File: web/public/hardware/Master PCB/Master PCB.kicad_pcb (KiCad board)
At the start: 2 copper layers, 73.5 x 77.1 mm, 110 parts, among them J1 SWD Conn, J10 LED3, J11 LDR4, J12 LED4, J13 LED Conn, J14 Relay Conn, J2 OLED1, J3 OLED2, J4 5V_IN, J5 LDR1, J6 LED1, J7 LDR2, J8 LED2, J9 LDR3, Q1 2N7000, Q2 2N7000, Q3 2N7000, Q4 2N7000, SW1 nRST, SW2 Menu Encoder, U1 STM32U585VITx, U2 M95P32-IXMNT, U3 TLV62568DBV, U4 LM339

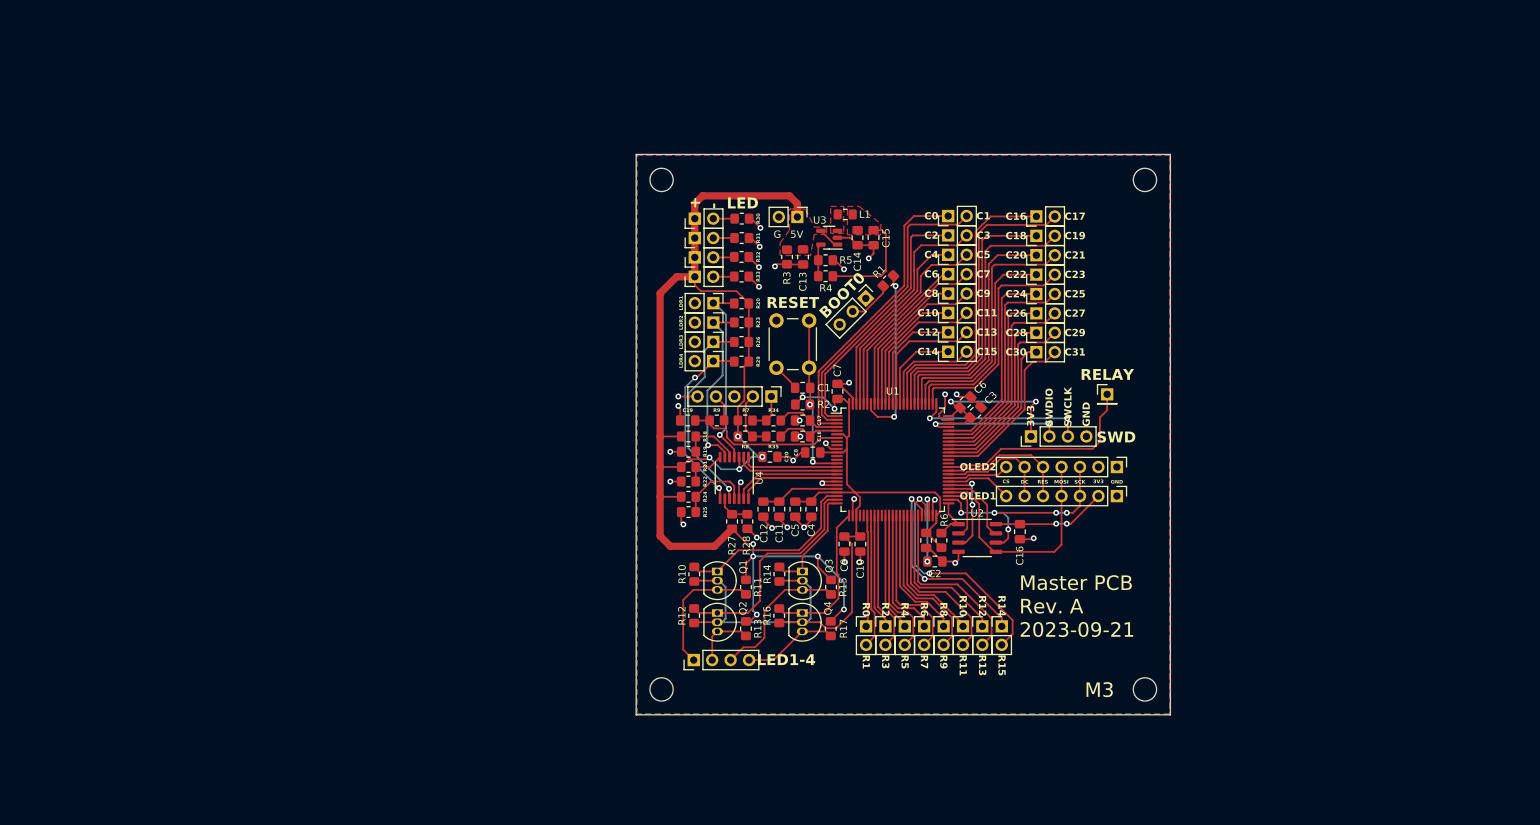
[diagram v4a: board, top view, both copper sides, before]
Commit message: Change STM32 pinout, begin placing components on new PCB
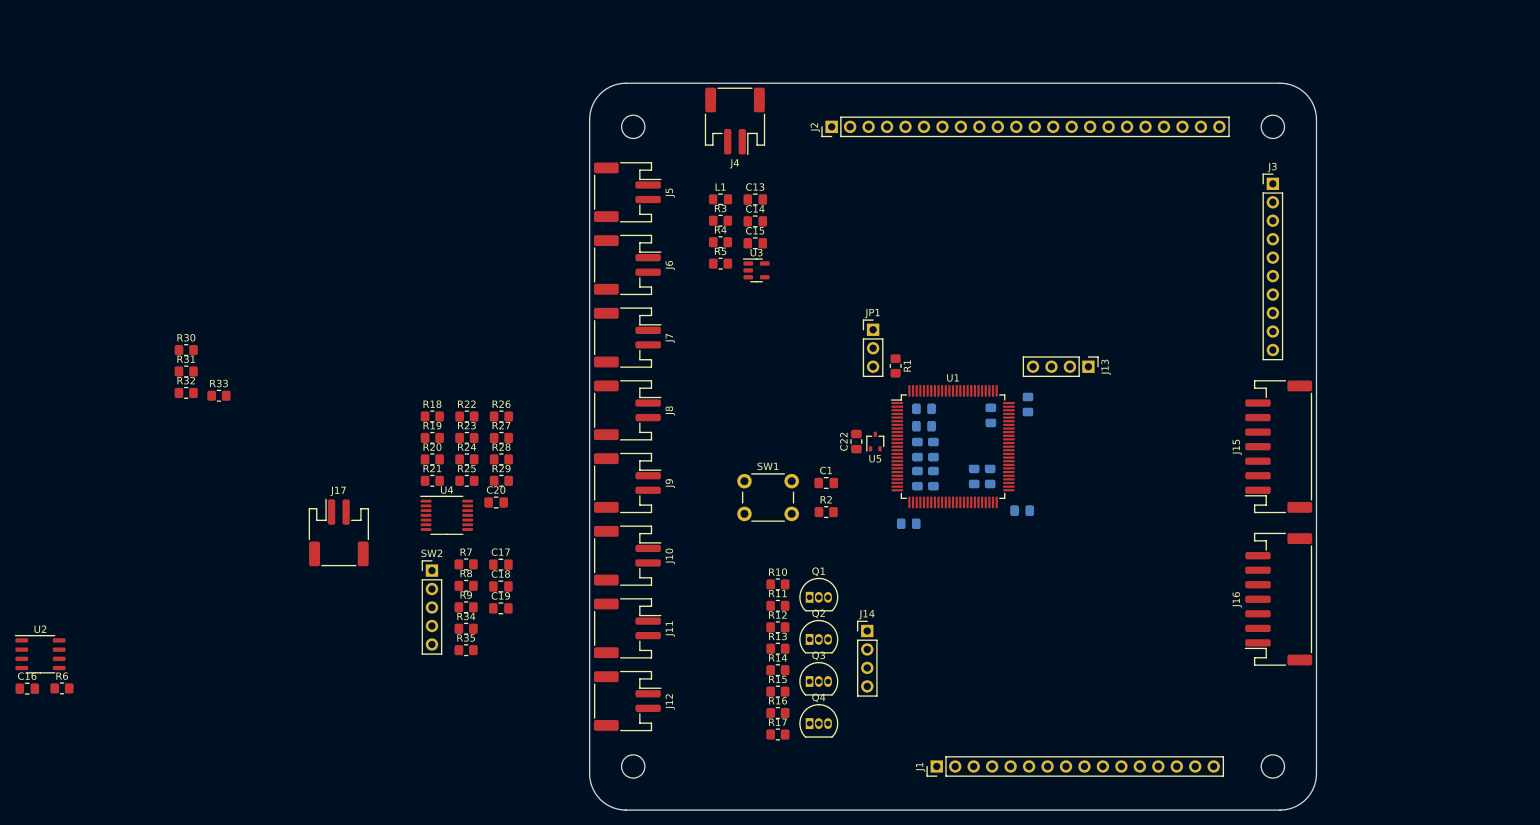
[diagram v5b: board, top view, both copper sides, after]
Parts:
- removed COL1: Cols 0-1, Connector_PinHeader_2.54mm:PinHeader_1x02_P2.54mm_Vertical
- removed COL10: Cols 18-19, Connector_PinHeader_2.54mm:PinHeader_1x02_P2.54mm_Vertical
- removed COL11: Cols 20-21, Connector_PinHeader_2.54mm:PinHeader_1x02_P2.54mm_Vertical
- removed COL12: Cols 22-23, Connector_PinHeader_2.54mm:PinHeader_1x02_P2.54mm_Vertical
- removed COL13: Cols 24-25, Connector_PinHeader_2.54mm:PinHeader_1x02_P2.54mm_Vertical
- removed COL14: Cols 26-27, Connector_PinHeader_2.54mm:PinHeader_1x02_P2.54mm_Vertical
- removed COL15: Cols 28-29, Connector_PinHeader_2.54mm:PinHeader_1x02_P2.54mm_Vertical
- removed COL16: Cols 30-31, Connector_PinHeader_2.54mm:PinHeader_1x02_P2.54mm_Vertical
- removed COL2: Cols 2-3, Connector_PinHeader_2.54mm:PinHeader_1x02_P2.54mm_Vertical
- removed COL3: Cols 4-5, Connector_PinHeader_2.54mm:PinHeader_1x02_P2.54mm_Vertical
- removed COL4: Cols 6-7, Connector_PinHeader_2.54mm:PinHeader_1x02_P2.54mm_Vertical
- removed COL5: Cols 8-9, Connector_PinHeader_2.54mm:PinHeader_1x02_P2.54mm_Vertical
- removed COL6: Cols 10-11, Connector_PinHeader_2.54mm:PinHeader_1x02_P2.54mm_Vertical
- removed COL7: Cols 12-13, Connector_PinHeader_2.54mm:PinHeader_1x02_P2.54mm_Vertical
- removed COL8: Cols 14-15, Connector_PinHeader_2.54mm:PinHeader_1x02_P2.54mm_Vertical
- removed COL9: Cols 16-17, Connector_PinHeader_2.54mm:PinHeader_1x02_P2.54mm_Vertical
- removed ROW1: Rows 0-1, Connector_PinHeader_2.54mm:PinHeader_1x02_P2.54mm_Vertical
- removed ROW2: Rows 2-3, Connector_PinHeader_2.54mm:PinHeader_1x02_P2.54mm_Vertical
- removed ROW3: Rows 4-5, Connector_PinHeader_2.54mm:PinHeader_1x02_P2.54mm_Vertical
- removed ROW4: Rows 6-7, Connector_PinHeader_2.54mm:PinHeader_1x02_P2.54mm_Vertical
- removed ROW5: Rows 8-9, Connector_PinHeader_2.54mm:PinHeader_1x02_P2.54mm_Vertical
- removed ROW6: Rows 10-11, Connector_PinHeader_2.54mm:PinHeader_1x02_P2.54mm_Vertical
- removed ROW7: Rows 12-13, Connector_PinHeader_2.54mm:PinHeader_1x02_P2.54mm_Vertical
- removed ROW8: Rows 14-15, Connector_PinHeader_2.54mm:PinHeader_1x02_P2.54mm_Vertical
- added C22: 100nF, Capacitor_SMD:C_0805_2012Metric_Pad1.18x1.45mm_HandSolder, F.Cu at (136.7, 99.3)
- added J15: OLED1, Connector_JST:JST_PH_S7B-PH-SM4-TB_1x07-1MP_P2.00mm_Horizontal, F.Cu at (194.8, 100.0)
- added J16: OLED2, Connector_JST:JST_PH_S7B-PH-SM4-TB_1x07-1MP_P2.00mm_Horizontal, F.Cu at (194.8, 121.0)
- added J17: Relay Conn, Connector_JST:JST_PH_S2B-PH-SM4-TB_1x02-1MP_P2.00mm_Horizontal, F.Cu at (65.5, 111.8)
- added U5: MAX7375AXR805, Package_TO_SOT_SMD:SOT-323_SC-70, F.Cu at (139.3, 99.3)
- C10, C11, C12, C2, C21, C3, C4, C5, C6, C7, C8, C9: moved to B.Cu
- J1: value SWD Conn -> Rows 0-15; footprint Connector_PinHeader_2.54mm:PinHeader_1x04_P2.54mm_Vertical -> Connector_PinHeader_2.54mm:PinHeader_1x16_P2.54mm_Vertical
- J10: value LED3 -> LDR2; footprint Connector_PinHeader_2.54mm:PinHeader_1x02_P2.54mm_Vertical -> Connector_JST:JST_PH_S2B-PH-SM4-TB_1x02-1MP_P2.00mm_Horizontal
- J11: value LDR4 -> LDR3; footprint Connector_PinHeader_2.54mm:PinHeader_1x02_P2.54mm_Vertical -> Connector_JST:JST_PH_S2B-PH-SM4-TB_1x02-1MP_P2.00mm_Horizontal
- J12: value LED4 -> LDR4; footprint Connector_PinHeader_2.54mm:PinHeader_1x02_P2.54mm_Vertical -> Connector_JST:JST_PH_S2B-PH-SM4-TB_1x02-1MP_P2.00mm_Horizontal
- J13: value LED Conn -> SWD Conn
- J14: value Relay Conn -> LED Conn; footprint Connector_PinHeader_2.54mm:PinHeader_1x01_P2.54mm_Vertical -> Connector_PinHeader_2.54mm:PinHeader_1x04_P2.54mm_Vertical
- J2: value OLED1 -> Cols 0-21; footprint Connector_PinHeader_2.54mm:PinHeader_1x07_P2.54mm_Vertical -> Connector_PinHeader_2.54mm:PinHeader_1x22_P2.54mm_Vertical
- J3: value OLED2 -> Cols 22-31; footprint Connector_PinHeader_2.54mm:PinHeader_1x07_P2.54mm_Vertical -> Connector_PinHeader_2.54mm:PinHeader_1x10_P2.54mm_Vertical
- J4: footprint Connector_PinHeader_2.54mm:PinHeader_1x02_P2.54mm_Vertical -> Connector_JST:JST_PH_S2B-PH-SM4-TB_1x02-1MP_P2.00mm_Horizontal
- J5: value LDR1 -> LED1; footprint Connector_PinHeader_2.54mm:PinHeader_1x02_P2.54mm_Vertical -> Connector_JST:JST_PH_S2B-PH-SM4-TB_1x02-1MP_P2.00mm_Horizontal
- J6: value LED1 -> LED2; footprint Connector_PinHeader_2.54mm:PinHeader_1x02_P2.54mm_Vertical -> Connector_JST:JST_PH_S2B-PH-SM4-TB_1x02-1MP_P2.00mm_Horizontal
- J7: value LDR2 -> LED3; footprint Connector_PinHeader_2.54mm:PinHeader_1x02_P2.54mm_Vertical -> Connector_JST:JST_PH_S2B-PH-SM4-TB_1x02-1MP_P2.00mm_Horizontal
- J8: value LED2 -> LED4; footprint Connector_PinHeader_2.54mm:PinHeader_1x02_P2.54mm_Vertical -> Connector_JST:JST_PH_S2B-PH-SM4-TB_1x02-1MP_P2.00mm_Horizontal
- J9: value LDR3 -> LDR1; footprint Connector_PinHeader_2.54mm:PinHeader_1x02_P2.54mm_Vertical -> Connector_JST:JST_PH_S2B-PH-SM4-TB_1x02-1MP_P2.00mm_Horizontal
- moved C16 138.3 mm to (22.6, 133.3), turned to 0 degrees
- moved U2 129.9 mm to (24.4, 128.6)
- moved R6 122.7 mm to (27.4, 133.3), turned to 0 degrees
- moved R32 78.7 mm to (44.5, 92.6)
- moved R31 78.6 mm to (44.5, 89.7)
- moved R30 78.6 mm to (44.5, 86.7)
- moved R33 73.7 mm to (49.0, 93.0)
- moved J13 67.7 mm to (168.6, 89.0), turned to -90 degrees
- moved J2 64.2 mm to (133.3, 56.0), turned to 90 degrees
- moved J12 59.1 mm to (105.2, 135.0), turned to -90 degrees
- moved SW2 52.5 mm to (78.3, 117.0), turned to 0 degrees
- moved R35 51.5 mm to (83.0, 128.0), turned to 0 degrees
- moved R34 51.1 mm to (83.0, 125.0), turned to 0 degrees
- moved R20 47.6 mm to (78.4, 101.8), turned to 0 degrees
- moved J1 47.2 mm to (147.8, 144.0)
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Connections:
- J1 pad 1: +3V3 -> /ROW0
- J1 pad 2: /STM32/SWDIO -> /ROW1
- J1 pad 3: /STM32/SWCLK -> /ROW2
- J1 pad 4: GND -> /ROW3
- J10 pad 1: +5V -> /Goal Detector/LDR2IN
- J10 pad 2: Net-(J10-Pin_2) -> GND
- J11 pad 1: /Goal Detector/LDR4IN -> /Goal Detector/LDR3IN
- J12 pad 1: +5V -> /Goal Detector/LDR4IN
- J12 pad 2: Net-(J12-Pin_2) -> GND
- J13 pad 1: /LED/LED1OUT -> +3V3
- J13 pad 2: /LED/LED2OUT -> /STM32/SWDIO
- J13 pad 3: /LED/LED3OUT -> /STM32/SWCLK
- J13 pad 4: /LED/LED4OUT -> GND
- J14 pad 1: /STM32/RELAY -> /LED/LED1OUT
- J2 pad 1: GND -> /COL0
- J2 pad 2: +3V3 -> /COL1
- J2 pad 3: /SPI2SCK -> /COL2
- J2 pad 4: /SPI2MOSI -> /COL3
- J2 pad 5: /OLEDRES -> /COL4
- J2 pad 6: /OLED1DC -> /COL5
- J2 pad 7: /OLED1CS -> /COL6
- J3 pad 1: GND -> /COL22
- J3 pad 2: +3V3 -> /COL23
- J3 pad 3: /SPI2SCK -> /COL24
- J3 pad 4: /SPI2MOSI -> /COL25
- J3 pad 5: /OLEDRES -> /COL26
- J3 pad 6: /OLED1DC -> /COL27
- J3 pad 7: /OLED2CS -> /COL28
- J5 pad 1: /Goal Detector/LDR1IN -> +5V
- J5 pad 2: GND -> Net-(J5-Pin_2)
- J7 pad 1: /Goal Detector/LDR2IN -> +5V
- J7 pad 2: GND -> Net-(J7-Pin_2)
- J9 pad 1: /Goal Detector/LDR3IN -> /Goal Detector/LDR1IN
- R30 pad 1: Net-(J6-Pin_2) -> Net-(J5-Pin_2)
- R31 pad 1: Net-(J8-Pin_2) -> Net-(J6-Pin_2)
- R32 pad 1: Net-(J10-Pin_2) -> Net-(J7-Pin_2)
- R33 pad 1: Net-(J12-Pin_2) -> Net-(J8-Pin_2)
- U1 pad 1: /COL2 -> /COL0
- U1 pad 15: /Goal Detector/LDR2OUT -> /STM32/DEBUG1
- U1 pad 16: /Goal Detector/LDR1OUT -> /STM32/DEBUG2
- U1 pad 17: /Goal Detector/LDR3OUT -> /STM32/DEBUG3
- U1 pad 18: /Goal Detector/LDR4OUT -> /STM32/DEBUG4
- U1 pad 2: /COL1 -> /Menu Encoder/ENCODER_A
- U1 pad 3: /COL0 -> /Menu Encoder/ENCODER_B
- U1 pad 4: /Menu Encoder/ENCODER_A -> /Menu Encoder/ENCODER_SW
- U1 pad 5: /Menu Encoder/ENCODER_B -> /Goal Detector/LDR1OUT
- U1 pad 59: /OLED1DC -> /OLEDDC
- U1 pad 62: unconnected-(U1-PD15-Pad62) -> /COL31
- U1 pad 63: unconnected-(U1-PC6-Pad63) -> /COL30
- U1 pad 64: /COL31 -> /COL29
- U1 pad 65: /COL30 -> /COL28
- U1 pad 66: /COL29 -> /COL27
- U1 pad 67: /COL28 -> /COL26
- U1 pad 68: /COL27 -> /COL25
- U1 pad 69: /COL26 -> /COL24
- U1 pad 7: /Menu Encoder/ENCODER_SW -> /Goal Detector/LDR2OUT
- U1 pad 70: /COL25 -> /COL23
- U1 pad 71: /COL24 -> /COL22
- U1 pad 77: /COL23 -> /COL21
- U1 pad 78: /COL22 -> /COL20
- U1 pad 79: /COL21 -> /COL19
- U1 pad 8: /STM32/OSC32_IN -> /Goal Detector/LDR3OUT
- U1 pad 80: /COL20 -> /COL18
- U1 pad 81: /COL19 -> /COL17
- U1 pad 82: /COL18 -> /COL16
- U1 pad 83: /COL17 -> /COL15
- U1 pad 84: /COL16 -> /COL14
- U1 pad 85: /COL15 -> /COL13
- U1 pad 86: /COL14 -> /COL12
- U1 pad 87: /COL13 -> /COL11
- U1 pad 88: /COL12 -> /COL10
- U1 pad 89: /COL11 -> /COL9
- U1 pad 9: /STM32/OSC32_OUT -> /Goal Detector/LDR4OUT
- U1 pad 90: /COL10 -> /COL8
- U1 pad 91: /COL9 -> /COL7
- U1 pad 92: /COL8 -> /COL6
- U1 pad 93: /COL7 -> /COL5
- U1 pad 95: /COL6 -> /COL4
- U1 pad 96: /COL5 -> /COL3
- U1 pad 97: /COL4 -> /COL2
- U1 pad 98: /COL3 -> /COL1
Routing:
- net +3V3: track 180.6 -> 0.00 mm, vias 6 -> 0
- net +5V: track 180.4 -> 0.00 mm, vias 9 -> 0
- net GND: track 89.5 -> 0.00 mm, vias 31 -> 0
- net /COL17: track 42.9 -> 0.00 mm
- net /COL1: track 41.8 -> 0.00 mm
- net /COL0: track 41.0 -> 0.00 mm
- net /COL16: track 40.9 -> 0.00 mm
- net /COL19: track 39.3 -> 0.00 mm
- net /COL18: track 38.1 -> 0.00 mm
- net /COL2: track 36.1 -> 0.00 mm
- net /COL21: track 35.4 -> 0.00 mm
- net /COL20: track 34.0 -> 0.00 mm
- net /SPI2MOSI: track 32.7 -> 0.00 mm
- net /ROW15: track 32.5 -> 0.00 mm, vias 2 -> 0
- net /COL3: track 32.4 -> 0.00 mm
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- removed copper zone on F.Cu, net +3V3
- removed copper zone on F.Cu, net +5V
- removed copper zone on B.Cu, net GND
- removed copper zone on F.Cu, net Net-(U3-SW)
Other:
- board size 73.5 x 77.1 mm -> 100 x 100 mm
- board text removed: "+"
- board text removed: "-"
- board text removed: "3V3"
- board text removed: "5V"
- board text removed: "BOOT0"
- board text removed: "C0"
- board text removed: "C1"
- board text removed: "C10"
- board text removed: "C11"
- board text removed: "C12"
- board text removed: "C13"
- board text removed: "C14"
- board text removed: "C15"
- board text removed: "C16"
- board text removed: "C17"
- board text removed: "C18"
- board text removed: "C19"
- board text removed: "C2"
- board text removed: "C20"
- board text removed: "C21"
- board text removed: "C22"
- board text removed: "C23"
- board text removed: "C24"
- board text removed: "C25"
- board text removed: "C26"
- board text removed: "C27"
- board text removed: "C28"
- board text removed: "C29"
- board text removed: "C3"
- board text removed: "C30"
- board text removed: "C31"
- board text removed: "C4"
- board text removed: "C5"
- board text removed: "C6"
- board text removed: "C7"
- board text removed: "C8"
- board text removed: "C9"
- board text removed: "CS"
- board text removed: "DC"
- board text removed: "G"
- board text removed: "GND"
- board text removed: "LDR1"
- board text removed: "LDR2"
- board text removed: "LDR3"
- board text removed: "LDR4"
- board text removed: "LED"
- board text removed: "LED1-4"
- board text removed: "M3"
- board text removed: "MOSI"
- board text removed: "Master PCB Rev. A 2023-09-21"
- board text removed: "OLED1"
- board text removed: "OLED2"
- board text removed: "R0"
- board text removed: "R1"
- board text removed: "R10"
- board text removed: "R11"
- board text removed: "R12"
- board text removed: "R13"
- board text removed: "R14"
- board text removed: "R15"
- board text removed: "R2"
- board text removed: "R3"
- board text removed: "R4"
- board text removed: "R5"
- board text removed: "R6"
- board text removed: "R7"
- board text removed: "R8"
- board text removed: "R9"
- board text removed: "RELAY"
- board text removed: "RES"
- board text removed: "RESET"
- board text removed: "SCK"
- board text removed: "SWCLK"
- board text removed: "SWD"
- board text removed: "SWDIO"

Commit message: Switch JST to THT
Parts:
- J10, J11, J12, J17, J4, J5, J6, J7, J8, J9: footprint Connector_JST:JST_PH_S2B-PH-SM4-TB_1x02-1MP_P2.00mm_Horizontal -> Connector_JST:JST_PH_B2B-PH-K_1x02_P2.00mm_Vertical
- J15, J16: footprint Connector_JST:JST_PH_S7B-PH-SM4-TB_1x07-1MP_P2.00mm_Horizontal -> Connector_JST:JST_PH_B7B-PH-K_1x07_P2.00mm_Vertical
- moved J17 130.6 mm to (195.0, 95.0), turned to -90 degrees
- moved J15 21.0 mm to (195.0, 121.0), turned to -90 degrees
- moved J16 18.0 mm to (195.0, 103.0), turned to -90 degrees
- moved J12 12.0 mm to (105.0, 123.0), turned to 90 degrees
- moved J11 10.0 mm to (105.0, 115.0), turned to 90 degrees
- moved J10 8.00 mm to (105.0, 107.0), turned to 90 degrees
- moved J9 6.00 mm to (105.0, 99.0), turned to 90 degrees
- moved J8 4.00 mm to (105.0, 91.0), turned to 90 degrees
- moved J5 2.01 mm to (105.0, 67.0), turned to 90 degrees
- moved J7 2.01 mm to (105.0, 83.0), turned to 90 degrees
- moved J4 1.02 mm to (119.0, 55.0), turned to 0 degrees
- moved J6 0.20 mm to (105.0, 75.0), turned to 90 degrees

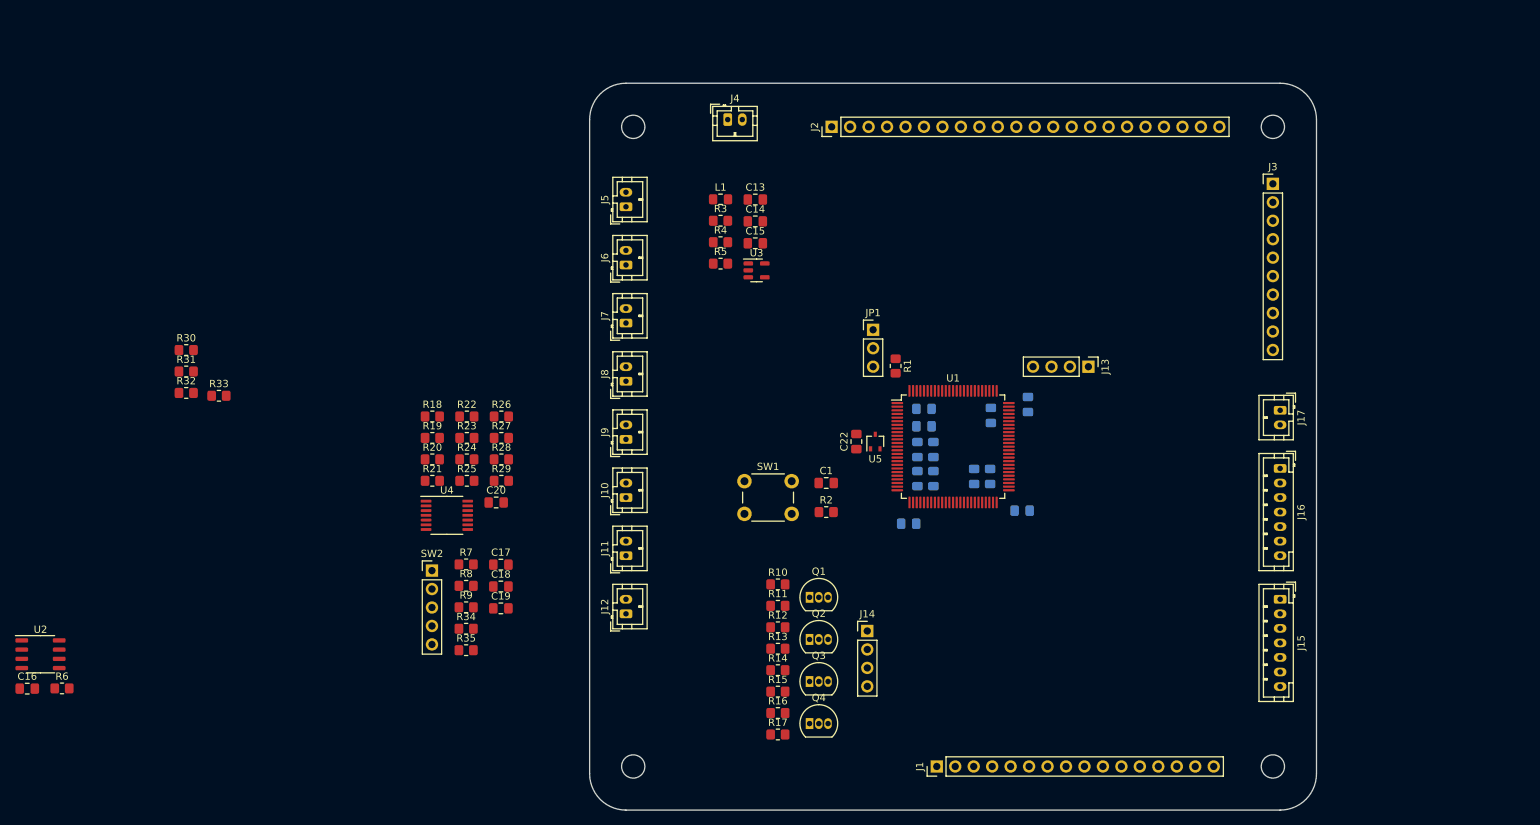
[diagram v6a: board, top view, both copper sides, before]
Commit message: Add ESD ICs and route part of board
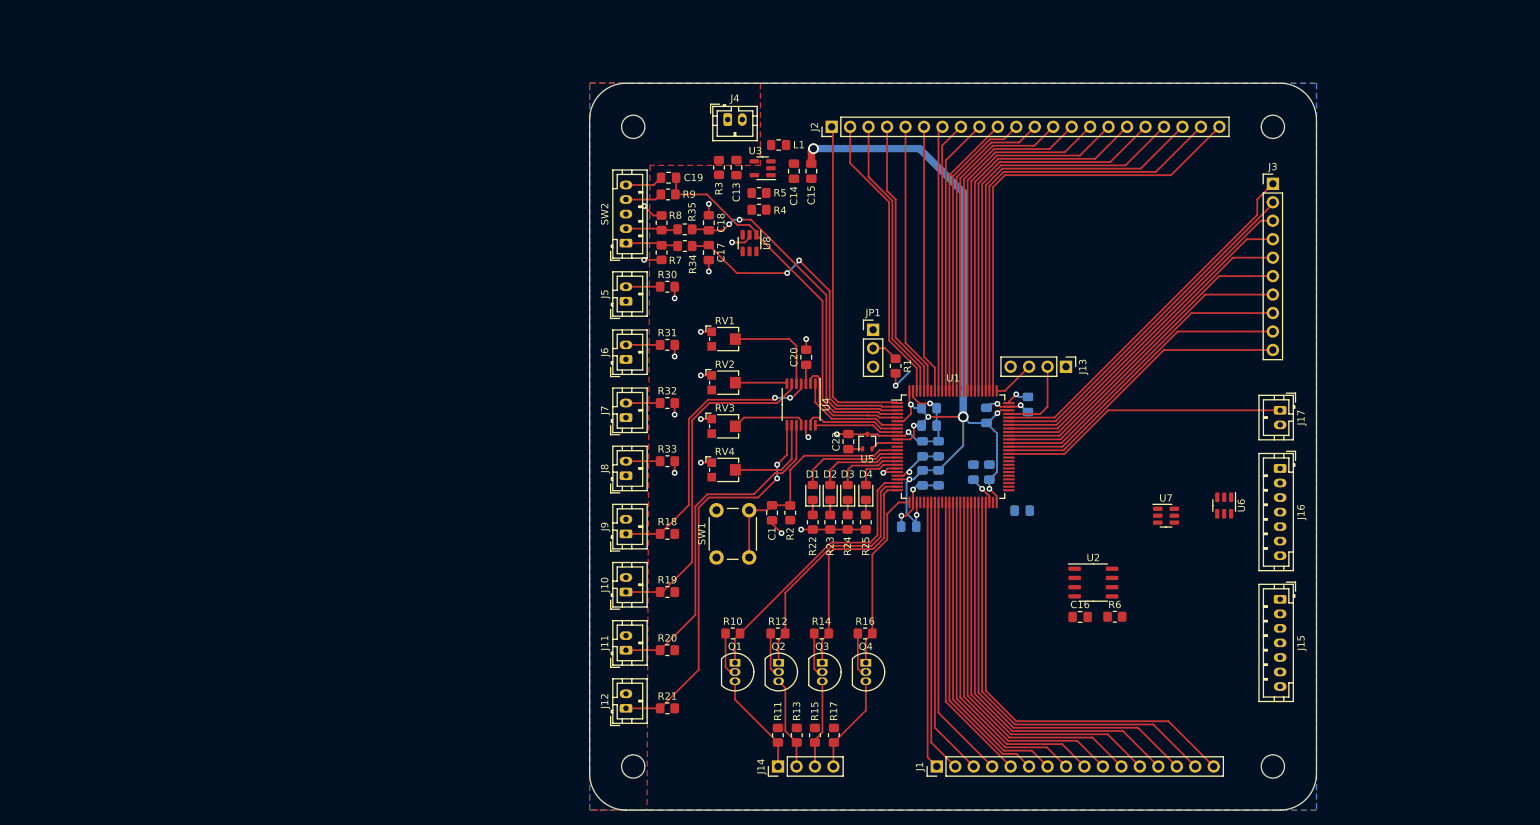
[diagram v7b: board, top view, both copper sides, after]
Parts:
- removed R26, R27, R28, R29: 10K, Resistor_SMD:R_0805_2012Metric_Pad1.20x1.40mm_HandSolder
- added D1: RED, LED_SMD:LED_0805_2012Metric_Pad1.15x1.40mm_HandSolder, F.Cu at (130.7, 106.3)
- added D2: YLW, LED_SMD:LED_0805_2012Metric_Pad1.15x1.40mm_HandSolder, F.Cu at (133.1, 106.3)
- added D3: GRN, LED_SMD:LED_0805_2012Metric_Pad1.15x1.40mm_HandSolder, F.Cu at (135.5, 106.3)
- added D4: BLU, LED_SMD:LED_0805_2012Metric_Pad1.15x1.40mm_HandSolder, F.Cu at (138.0, 106.3)
- added RV1: 10K, Potentiometer_SMD:Potentiometer_Bourns_TC33X_Vertical, F.Cu at (118.6, 85.2)
- added RV2: 10K, Potentiometer_SMD:Potentiometer_Bourns_TC33X_Vertical, F.Cu at (118.6, 91.2)
- added RV3: 10K, Potentiometer_SMD:Potentiometer_Bourns_TC33X_Vertical, F.Cu at (118.6, 97.2)
- added RV4: 10K, Potentiometer_SMD:Potentiometer_Bourns_TC33X_Vertical, F.Cu at (118.6, 103.2)
- added U6: USBLC6-4SC6, Package_TO_SOT_SMD:SOT-23-6, F.Cu at (187.3, 108.1)
- added U7: USBLC6-2SC6, Package_TO_SOT_SMD:SOT-23-6, F.Cu at (179.3, 109.5)
- added U8: USBLC6-2SC6, Package_TO_SOT_SMD:SOT-23-6, F.Cu at (122.0, 72.0)
- R22, R23, R24, R25: value 10K -> 100
- SW2: footprint Connector_PinHeader_2.54mm:PinHeader_1x05_P2.54mm_Vertical -> Connector_JST:JST_PH_B5B-PH-K_1x05_P2.00mm_Vertical
- moved U2 145.2 mm to (169.3, 118.7)
- moved C16 145.2 mm to (167.5, 123.4)
- moved R6 145.2 mm to (172.3, 123.4)
- moved R30 66.8 mm to (110.7, 78.0)
- moved R31 66.3 mm to (110.7, 86.0)
- moved R32 66.2 mm to (110.7, 94.0)
- moved R35 65.3 mm to (113.1, 70.1), turned to 180 degrees
- moved C19 63.6 mm to (110.9, 63.0), turned to 180 degrees
- moved R9 63.2 mm to (110.8, 65.3)
- moved R33 62.4 mm to (110.7, 102.0)
- moved R34 60.6 mm to (113.1, 72.4), turned to 180 degrees
- moved C18 57.6 mm to (116.4, 69.2), turned to 90 degrees
- moved R8 56.7 mm to (109.9, 69.2), turned to -90 degrees
- moved R25 55.2 mm to (138.0, 110.4), turned to -90 degrees
- moved R24 53.1 mm to (135.5, 110.4), turned to -90 degrees
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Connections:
- R18 pad 1: +5V -> /Goal Detector/LDR1IN
- R18 pad 2: Net-(U4A-+) -> +5V
- R19 pad 1: GND -> /Goal Detector/LDR2IN
- R19 pad 2: Net-(U4A-+) -> +5V
- R20 pad 1: +5V -> /Goal Detector/LDR3IN
- R20 pad 2: /Goal Detector/LDR1IN -> +5V
- R21 pad 1: +5V -> /Goal Detector/LDR4IN
- R21 pad 2: Net-(U4B-+) -> +5V
- R22 pad 1: GND -> Net-(D1-K)
- R22 pad 2: Net-(U4B-+) -> GND
- R23 pad 1: +5V -> Net-(D2-K)
- R23 pad 2: /Goal Detector/LDR2IN -> GND
- R24 pad 1: +5V -> Net-(D3-K)
- R24 pad 2: Net-(U4C-+) -> GND
- R25 pad 1: GND -> Net-(D4-K)
- R25 pad 2: Net-(U4C-+) -> GND
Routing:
- net +3V3: track 0.00 -> 151.5 mm, vias 0 -> 10
- net GND: track 0.00 -> 83.1 mm, vias 0 -> 23
- net /COL21: track 0.00 -> 62.6 mm
- net /ROW15: track 0.00 -> 61.6 mm
- net /COL20: track 0.00 -> 60.6 mm
- net /ROW14: track 0.00 -> 59.6 mm
- net /COL19: track 0.00 -> 58.7 mm
- net /ROW13: track 0.00 -> 57.7 mm
- net /COL18: track 0.00 -> 56.7 mm
- net /ROW12: track 0.00 -> 55.7 mm
- net /Goal Detector/LDR4IN: track 0.00 -> 54.8 mm, vias 0 -> 2
- net /COL17: track 0.00 -> 54.8 mm
- net /ROW11: track 0.00 -> 53.7 mm
- net /Menu Encoder/ENCODER_SW: track 0.00 -> 53.5 mm
- net /COL16: track 0.00 -> 52.8 mm
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- added copper zone on F.Cu, net +5V
- added copper zone on B.Cu, net GND

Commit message: Finish routing
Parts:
- RV1, RV2, RV3, RV4: footprint Potentiometer_SMD:Potentiometer_Bourns_TC33X_Vertical -> Potentiometer_THT:Potentiometer_Bourns_3296W_Vertical
- moved U7 15.5 mm to (186.0, 123.5), turned to 180 degrees
- moved C16 11.7 mm to (163.5, 112.4), turned to 180 degrees
- moved U2 10.7 mm to (167.2, 108.2), turned to 180 degrees
- moved R6 10.4 mm to (169.8, 113.3), turned to 90 degrees
- moved RV1 3.54 mm to (122.1, 85.2)
- moved RV2 3.54 mm to (122.1, 91.2)
- moved RV3 3.54 mm to (122.1, 97.2)
- moved RV4 3.54 mm to (122.1, 103.2)
- moved U6 0.10 mm to (187.2, 108.1)
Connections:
- U6 pad 3: /OLEDRES -> /SPI2MOSI
- U6 pad 4: /SPI2MOSI -> /OLEDDC
- U6 pad 6: /OLEDDC -> /OLEDRES
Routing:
- net +3V3: track 151.5 -> 550.8 mm, vias 10 -> 22
- net +5V: track 7.96 -> 128.1 mm, vias 2 -> 18
- net /OLEDRES: track 0.00 -> 67.8 mm, vias 0 -> 4
- net /SPI2SCK: track 0.00 -> 65.5 mm, vias 0 -> 2
- net /OLEDDC: track 0.00 -> 63.2 mm, vias 0 -> 2
- net /SPI2MOSI: track 0.00 -> 63.0 mm, vias 0 -> 4
- net /OLED1CS: track 0.00 -> 52.3 mm
- net /OLED2CS: track 0.00 -> 50.8 mm
- net /EEPROM/MEMW: track 0.00 -> 16.7 mm
- net /EEPROM/MEM1CS: track 0.00 -> 16.0 mm
- net GND: track 83.1 -> 97.7 mm, vias 23 -> 28
- net /EEPROM/MEMHOLD: track 0.00 -> 13.8 mm, vias 0 -> 2
- net /MEMMISO: track 0.00 -> 13.7 mm
- net /STM32/BOOT0: track 4.39 -> 10.3 mm, vias 1 -> 2
- net Net-(U3-FB): track 0.00 -> 4.90 mm
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- added copper zone on F.Cu, net +3V3
- added copper zone on F.Cu, net Net-(U3-SW)
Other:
- board text added: "ECE 477 Group 5 Smart Air Hockey Table Master PCB Rev. B 2023-10-03 Alan Chung Ma William Doebert Trevor Moorman Ben Owen"
